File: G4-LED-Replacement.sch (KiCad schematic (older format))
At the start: 28 parts, among them J1 G4, J2 LED+, J3 LED-, Q1 DMN6075S-7, U1 LT3956

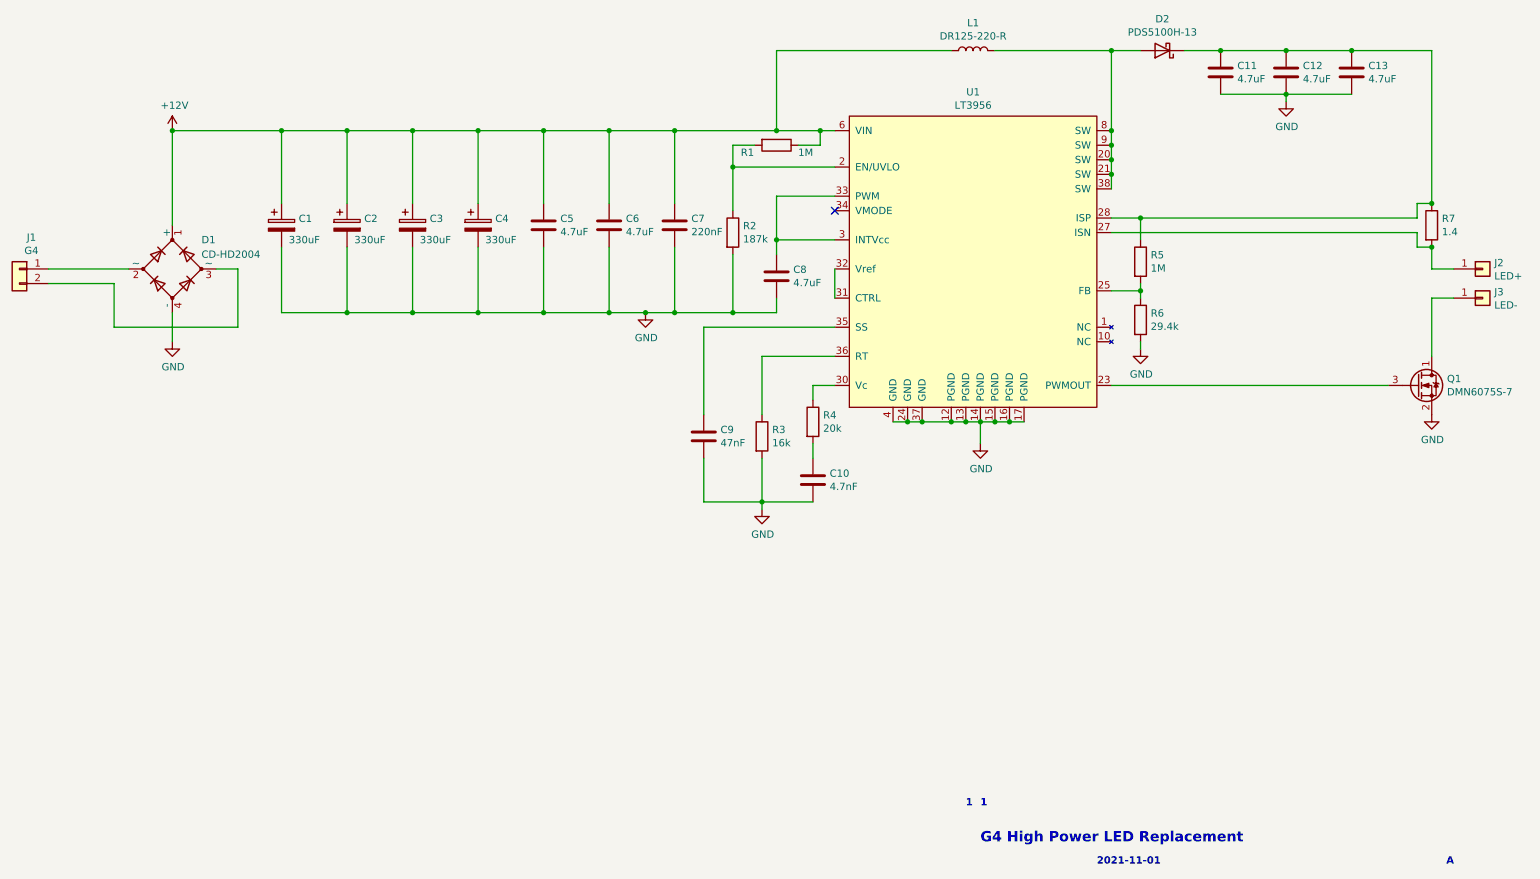
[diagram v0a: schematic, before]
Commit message: Added routed PCB
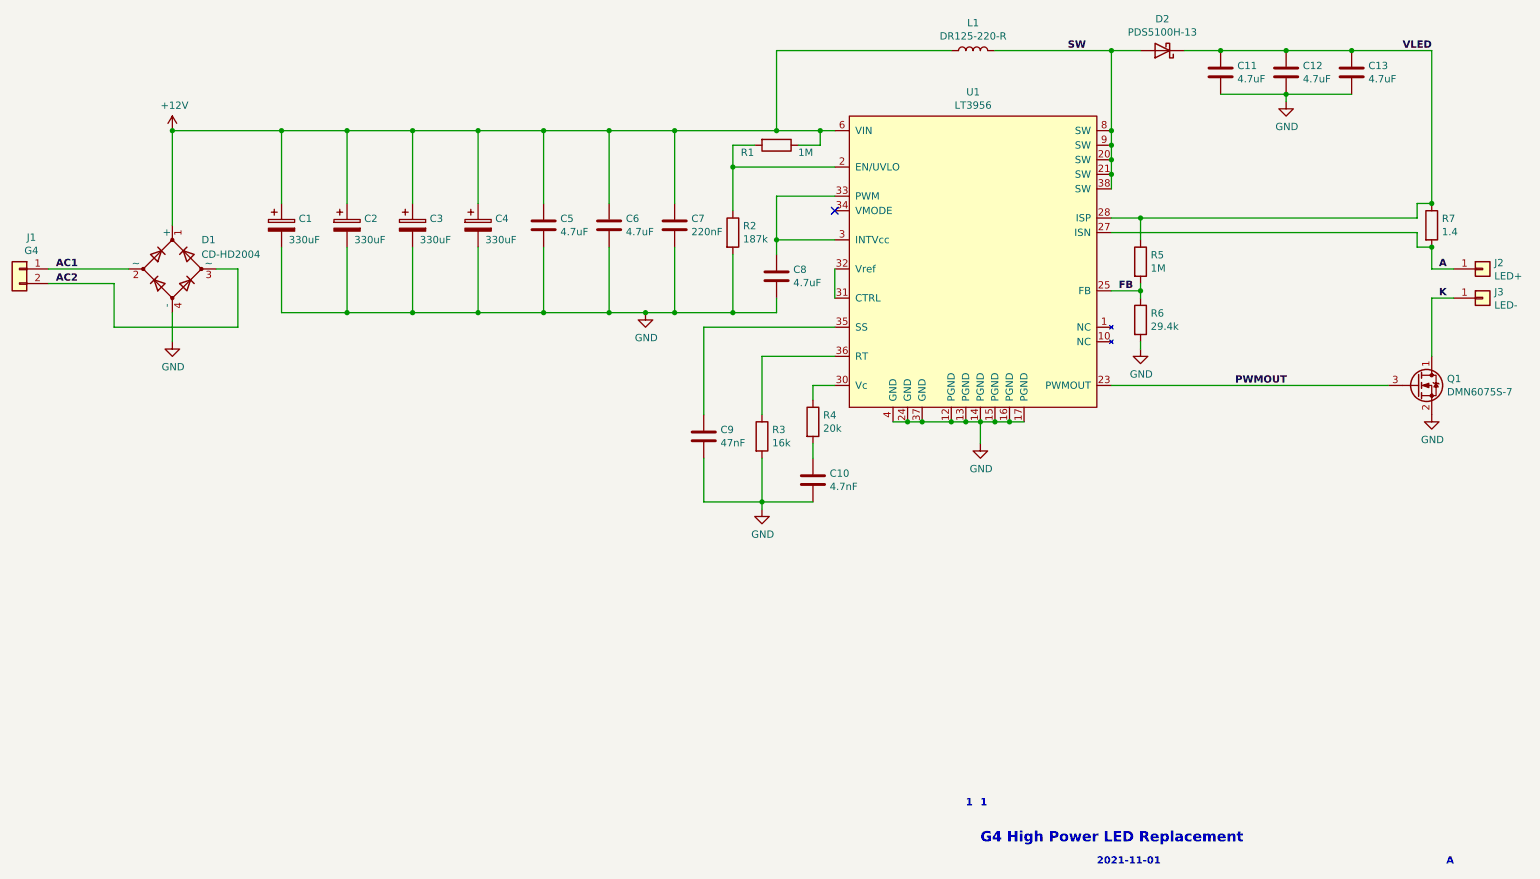
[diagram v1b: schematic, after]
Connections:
- net SW: now reaches D2.2 (A), L1.2, U1.20 (SW), U1.21 (SW), U1.38 (SW), U1.8 (SW), U1.9 (SW)
- net PWMOUT: now reaches Q1.3 (G), U1.23 (PWMOUT)
- net FB: now reaches R5.2, R6.1, U1.25 (FB)
- net A: now reaches J2.1 (Pin_1), R7.2, U1.27 (ISN)
- net VLED: now reaches C11.1, C12.1, C13.1, D2.1 (K), R5.1, R7.1, U1.28 (ISP)
- net AC1: now reaches D1.2 (~~), J1.1 (Pin_1)
- net AC2: now reaches D1.3 (~~), J1.2 (Pin_2)
- net K: now reaches J3.1 (Pin_1), Q1.1 (D)
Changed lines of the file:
@@
 Text Notes 7400 7250 0    50   ~ 10
 1
+Text Label 8000 2050 0    50   ~ 10
+SW
+Text Label 10300 2050 0    50   ~ 10
+VLED
+Text Label 10550 3550 0    50   ~ 10
+A
+Text Label 10550 3750 0    50   ~ 10
+K
+Text Label 9150 4350 0    50   ~ 10
+PWMOUT
+Text Label 8350 3700 0    50   ~ 10
+FB
+Text Label 1050 3550 0    50   ~ 10
+AC1
+Text Label 1050 3650 0    50   ~ 10
+AC2
 $EndSCHEMATC
